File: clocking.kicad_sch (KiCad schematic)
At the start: 37 parts, among them J9 U.Fl, U2 LMK05318BRGZR, U21 TMP117xxDRV, U3 TG5032CGN

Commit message: Minor updates.
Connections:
- net VDDO_PLL2 renamed VDD_PLL2
- net VDDO_XO renamed VDD_XO
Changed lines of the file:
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@@
 		)
 	)
-	(text_box "The variant with filter cap appears to be vapour-ware."
+	(text_box "The variant with external filter cap appears to be vapour-ware."
 		(exclude_from_sim no)
-		(at 212.1153 31.8079 0)
-		(size 30.4547 5.0221)
+		(at 212.1153 43.2379 0)
+		(size 19.0247 10.1021)
 		(margins 0.9525 0.9525 0.9525 0.9525)
 		(stroke
@@
 		)
 	)
-	(label "VDDO_PLL2"
+	(label "VDD_PLL2"
 		(at 218.44 66.04 270)
 		(effects
@@
 		)
 	)
-	(label "VDDO_XO"
+	(label "VDD_XO"
 		(at 91.44 110.49 180)
 		(effects
@@
 		)
 	)
-	(label "VDDO_XO"
+	(label "VDD_XO"
 		(at 238.76 97.79 180)
 		(effects
@@
 		)
 	)
-	(label "VDDO_PLL2"
+	(label "VDD_PLL2"
 		(at 120.65 93.98 180)
 		(effects

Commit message: Minor tidy ups and fix a stupid bug.
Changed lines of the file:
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@@
 	)
 	(junction
+		(at 69.85 34.29)
+		(diameter 0)
+		(color 0 0 0 0)
+	)
+	(junction
 		(at 190.5 133.35)
 		(diameter 0)
@@
 	)
 	(junction
+		(at 69.85 74.93)
+		(diameter 0)
+		(color 0 0 0 0)
+	)
+	(junction
 		(at 96.52 48.26)
 		(diameter 0)
@@
 	)
 	(junction
-		(at 69.85 81.28)
-		(diameter 0)
-		(color 0 0 0 0)
-	)
-	(junction
 		(at 115.57 60.96)
 		(diameter 0)
@@
 	(wire
 		(pts
-			(xy 66.04 81.28) (xy 69.85 81.28)
+			(xy 66.04 74.93) (xy 69.85 74.93)
 		)
 		(stroke
@@
 	(wire
 		(pts
-			(xy 66.04 48.26) (xy 69.85 48.26)
+			(xy 66.04 34.29) (xy 69.85 34.29)
 		)
 		(stroke
@@
 	(wire
 		(pts
-			(xy 69.85 74.93) (xy 69.85 81.28)
-		)
-		(stroke
-			(width 0)
-			(type default)
-		)
-	)
-	(wire
-		(pts
 			(xy 227.33 113.03) (xy 238.76 113.03)
 		)
@@
 	(wire
 		(pts
-			(xy 69.85 81.28) (xy 69.85 88.9)
+			(xy 69.85 74.93) (xy 69.85 88.9)
 		)
 		(stroke
@@
 	(symbol
 		(lib_id "power:+1V8")
-		(at 66.04 48.26 0)
+		(at 66.04 34.29 0)
 		(unit 1)
 		(exclude_from_sim no)
@@
 		(dnp no)
 		(property "Reference" "#PWR062"
-			(at 66.04 52.07 0)
+			(at 66.04 38.1 0)
 			(effects
 				(font
@@
 		)
 		(property "Value" "+1V8"
-			(at 66.04 44.704 0)
+			(at 66.04 30.734 0)
 			(effects
 				(font
@@
 		)
 		(property "Footprint" ""
-			(at 66.04 48.26 0)
+			(at 66.04 34.29 0)
 			(effects
 				(font
@@
 		)
 		(property "Datasheet" ""
-			(at 66.04 48.26 0)
+			(at 66.04 34.29 0)
 			(effects
 				(font
@@
 		)
 		(property "Description" "Power symbol creates a global label with name \"+1V8\""
-			(at 66.04 48.26 0)
+			(at 66.04 34.29 0)
 			(effects
 				(font
@@
 	(symbol
 		(lib_id "power:+3V3")
-		(at 66.04 81.28 0)
+		(at 66.04 74.93 0)
 		(unit 1)
 		(exclude_from_sim no)
@@
 		(dnp no)
 		(property "Reference" "#PWR011"
-			(at 66.04 85.09 0)
+			(at 66.04 78.74 0)
 			(effects
 				(font
@@
 		)
 		(property "Value" "+3V3"
-			(at 66.04 77.724 0)
+			(at 66.04 71.374 0)
 			(effects
 				(font
@@
 		)
 		(property "Footprint" ""
-			(at 66.04 81.28 0)
+			(at 66.04 74.93 0)
 			(effects
 				(font
@@
 		)
 		(property "Datasheet" ""
-			(at 66.04 81.28 0)
+			(at 66.04 74.93 0)
 			(effects
 				(font
@@
 		)
 		(property "Description" "Power symbol creates a global label with name \"+3V3\""
-			(at 66.04 81.28 0)
+			(at 66.04 74.93 0)
 			(effects
 				(font

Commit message: Add LCSC part numbers for a few items.
Don't 'exclude from BOM' things we want to assemble.
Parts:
- C78: LCSC (none) -> C3855387; now in the parts list
- C92: LCSC (none) -> C20044553; now in the parts list
- U2, U3: now in the parts list
- U21: now not fitted
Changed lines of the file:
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@@
 		(in_bom no)
 		(on_board yes)
-		(dnp no)
+		(dnp yes)
 		(property "Reference" "U21"
 			(at 107.95 135.763 0)
@@
 		)
 		(instances
-			(project ""
+			(project "gpsfreak"
 				(path "/3160ff17-81c2-4674-af97-e8d9acaf6b65/131a3728-0d51-4d75-9961-26d31d87be39"
 					(reference "U21")
@@
 		)
 		(instances
-			(project ""
+			(project "gpsfreak"
 				(path "/3160ff17-81c2-4674-af97-e8d9acaf6b65/131a3728-0d51-4d75-9961-26d31d87be39"
 					(reference "#PWR062")
@@
 		(unit 1)
 		(exclude_from_sim no)
-		(in_bom no)
+		(in_bom yes)
 		(on_board yes)
 		(dnp no)
@@
 			)
 		)
+		(property "LCSC" "C3855387"
+			(at 243.84 133.35 0)
+			(effects
+				(font
+					(size 1.27 1.27)
+				)
+				(hide yes)
+			)
+		)
 		(pin "1"
 		)
@@
 		)
 		(instances
-			(project ""
+			(project "gpsfreak"
 				(path "/3160ff17-81c2-4674-af97-e8d9acaf6b65/131a3728-0d51-4d75-9961-26d31d87be39"
 					(reference "L26")
@@
 		(unit 1)
 		(exclude_from_sim no)
-		(in_bom no)
+		(in_bom yes)
 		(on_board yes)
 		(dnp no)
@@
 		)
 		(instances
-			(project ""
+			(project "gpsfreak"
 				(path "/3160ff17-81c2-4674-af97-e8d9acaf6b65/131a3728-0d51-4d75-9961-26d31d87be39"
 					(reference "R24")
@@
 		(unit 1)
 		(exclude_from_sim no)
-		(in_bom no)
+		(in_bom yes)
 		(on_board yes)
 		(dnp no)
@@
 		(unit 2)
 		(exclude_from_sim no)
-		(in_bom no)
+		(in_bom yes)
 		(on_board yes)
 		(dnp no)
@@
 		)
 		(instances
-			(project ""
+			(project "gpsfreak"
 				(path "/3160ff17-81c2-4674-af97-e8d9acaf6b65/131a3728-0d51-4d75-9961-26d31d87be39"
 					(reference "U3")
@@
 		(unit 1)
 		(exclude_from_sim no)
-		(in_bom no)
+		(in_bom yes)
 		(on_board yes)
 		(dnp no)
@@
 			(effects
 				(font
+					(size 1.27 1.27)
+				)
+				(hide yes)
+			)
+		)
+		(property "LCSC" "C20044553"
+			(at 245.11 95.25 90)
+			(effects
+				(font

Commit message: Tweaks to python scripts.
Add part numbers for the LED and 470nF C0G capacitor.
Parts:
- C79: LCSC (none) -> C21082486
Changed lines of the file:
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@@
 		)
 	)
+	(text_box "Temperature sensor is optional."
+		(exclude_from_sim no)
+		(at 125.73 134.62 0)
+		(size 20.32 4.768)
+		(margins 0.9525 0.9525 0.9525 0.9525)
+		(stroke
+			(width 0)
+			(type solid)
+		)
+		(fill
+			(type none)
+		)
+		(effects
+			(font
+				(size 1.27 1.27)
+			)
+			(justify left)
+		)
+	)
 	(text_box "GPIO1 selects I²C address."
 		(exclude_from_sim no)
@@
 			)
 		)
-		(property "Description" "Unpolarized capacitor"
+		(property "Description" "GRM31C5C1E474"
+			(at 251.46 133.35 0)
+			(effects
+				(font
+					(size 1.27 1.27)
+				)
+				(hide yes)
+			)
+		)
+		(property "LCSC" "C21082486"
 			(at 251.46 133.35 0)
 			(effects

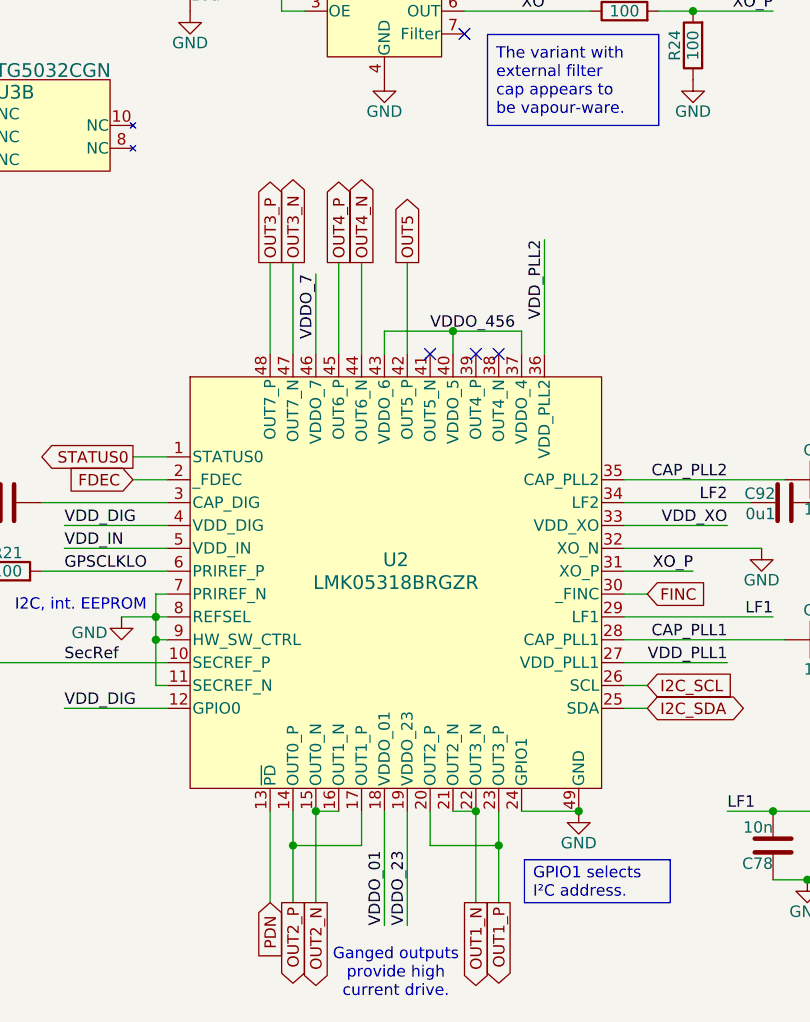
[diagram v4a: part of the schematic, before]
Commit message: Split each output onto it's own sheet.
Makes it easier to mix'n'match output types for board spins.
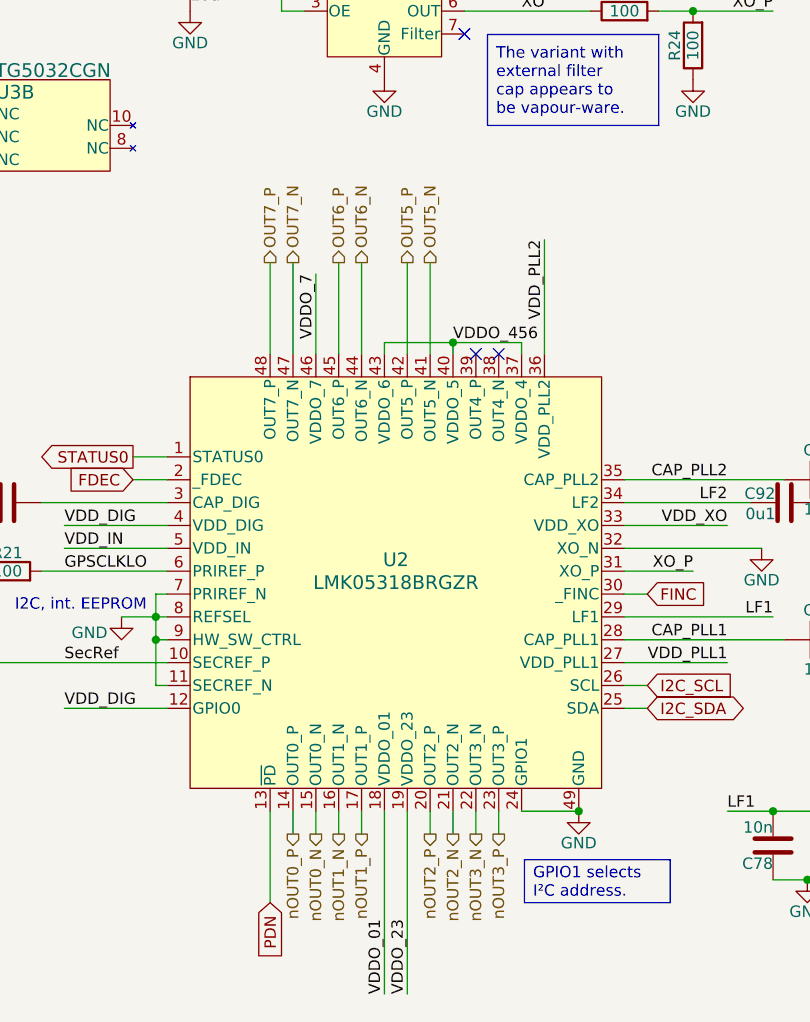
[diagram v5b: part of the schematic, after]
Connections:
- net OUT5_N: now reaches U2.41 (OUT5_N)
- net OUT1_N renamed nOUT2_N
- net nOUT2_N: no longer U2.22 (OUT3_N)
- net OUT1_P renamed nOUT2_P
- net nOUT2_P: no longer U2.23 (OUT3_P)
- net OUT2_N renamed nOUT0_N
- net nOUT0_N: no longer U2.16 (OUT1_N)
- net OUT2_P renamed nOUT0_P
- net nOUT0_P: no longer U2.17 (OUT1_P)
- net OUT3_N renamed OUT7_N
- net OUT3_P renamed OUT7_P
- net OUT4_N renamed OUT6_N
- net OUT4_P renamed OUT6_P
- net OUT5 renamed OUT5_P
- new net nOUT1_N: U2.16 (OUT1_N)
- new net nOUT1_P: U2.17 (OUT1_P)
- new net nOUT3_N: U2.22 (OUT3_N)
- new net nOUT3_P: U2.23 (OUT3_P)
- no-connect marks 4 -> 3
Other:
- note removed: "Ganged outputs provide high current drive."

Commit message: Touch up net names.
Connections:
- net OUT4_N: now reaches U2.38 (OUT4_N)
- net OUT4_P: now reaches U2.39 (OUT4_P)
- net nOUT0_N renamed OUT0_N
- net nOUT0_P renamed OUT0_P
- net nOUT1_N renamed OUT1_N
- net nOUT1_P renamed OUT1_P
- net nOUT2_N renamed OUT2_N
- net nOUT2_P renamed OUT2_P
- net nOUT3_N renamed OUT3_N
- net nOUT3_P renamed OUT3_P
- no-connect marks 3 -> 1
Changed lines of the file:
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@@
-	)
-	(no_connect
-		(at 213.36 78.74)
 	)
 	(no_connect
 		(at 209.55 43.18)
 	)
-	(no_connect
-		(at 210.82 78.74)
-	)
 	(wire
 		(pts
@@
 	(wire
 		(pts
-			(xy 205.74 68.58) (xy 205.74 78.74)
+			(xy 205.74 76.2) (xy 205.74 78.74)
 		)
 		(stroke
@@
 	(wire
 		(pts
-			(xy 195.58 78.74) (xy 195.58 68.58)
+			(xy 195.58 78.74) (xy 195.58 76.2)
 		)
 		(stroke
@@
 	(wire
 		(pts
+			(xy 213.36 76.2) (xy 213.36 78.74)
+		)
+		(stroke
+			(width 0)
+			(type default)
+		)
+	)
+	(wire
+		(pts
 			(xy 210.82 129.54) (xy 210.82 132.08)
 		)
@@
 	(wire
 		(pts
+			(xy 208.28 57.15) (xy 208.28 77.47)
+		)
+		(stroke
+			(width 0)
+			(type default)
+		)
+	)
+	(wire
+		(pts
 			(xy 254 95.25) (xy 254 110.49)
 		)
@@
 	(wire
 		(pts
-			(xy 190.5 78.74) (xy 190.5 68.58)
+			(xy 190.5 78.74) (xy 190.5 76.2)
 		)
 		(stroke
@@
 	(wire
 		(pts
-			(xy 193.04 78.74) (xy 193.04 69.85)
+			(xy 193.04 78.74) (xy 193.04 59.69)
 		)
 		(stroke
@@
 	(wire
 		(pts
-			(xy 203.2 68.58) (xy 203.2 78.74)
+			(xy 203.2 76.2) (xy 203.2 78.74)
 		)
 		(stroke
@@
 	(wire
 		(pts
-			(xy 198.12 78.74) (xy 198.12 68.58)
+			(xy 198.12 78.74) (xy 198.12 76.2)
 		)
 		(stroke
@@
 	(wire
 		(pts
-			(xy 187.96 78.74) (xy 187.96 68.58)
+			(xy 187.96 78.74) (xy 187.96 76.2)
 		)
 		(stroke
@@
 		(pts
 			(xy 107.95 146.05) (xy 119.38 146.05)
+		)
+		(stroke
+			(width 0)
+			(type default)
+		)
+	)
+	(wire
+		(pts
+			(xy 210.82 76.2) (xy 210.82 78.74)
 		)
 		(stroke
@@
 	)
 	(label "VDDO_456"
-		(at 208.28 77.47 0)
-		(effects
-			(font
-				(size 1.27 1.27)
-			)
-			(justify left bottom)
+		(at 208.28 57.15 270)
+		(effects
+			(font
+				(size 1.27 1.27)
+			)
+			(justify right bottom)
 		)
 	)
@@
 	)
 	(label "VDDO_7"
-		(at 193.04 69.85 270)
+		(at 193.04 59.69 270)
 		(effects
 			(font
@@
 	(hierarchical_label "OUT7_P"
 		(shape output)
-		(at 187.96 68.58 90)
+		(at 187.96 76.2 90)
 		(effects
 			(font
@@
 		)
 	)
-	(hierarchical_label "nOUT0_P"
+	(hierarchical_label "OUT0_P"
 		(shape output)
 		(at 190.5 132.08 270)
@@
 		)
 	)
-	(hierarchical_label "nOUT3_N"
+	(hierarchical_label "OUT3_N"
 		(shape output)
 		(at 210.82 132.08 270)
@@
 	(hierarchical_label "OUT6_N"
 		(shape output)
-		(at 198.12 68.58 90)
+		(at 198.12 76.2 90)
 		(effects
 			(font
@@
 		)
 	)
-	(hierarchical_label "nOUT2_N"
+	(hierarchical_label "OUT2_N"
 		(shape output)
 		(at 208.28 132.08 270)
@@
 		)
 	)
-	(hierarchical_label "nOUT2_P"
+	(hierarchical_label "OUT2_P"
 		(shape output)
 		(at 205.74 132.08 270)
@@
 	(hierarchical_label "OUT7_N"
 		(shape output)
-		(at 190.5 68.58 90)
+		(at 190.5 76.2 90)
 		(effects
 			(font
@@
 		)
 	)
-	(hierarchical_label "nOUT3_P"
+	(hierarchical_label "OUT4_N"
+		(shape output)
+		(at 213.36 76.2 90)
+		(effects
+			(font
+				(size 1.27 1.27)
+			)
+			(justify left)
+		)
+	)
+	(hierarchical_label "OUT3_P"
 		(shape output)
 		(at 213.36 132.08 270)
@@
 		)
 	)
-	(hierarchical_label "nOUT1_P"
+	(hierarchical_label "OUT1_P"
 		(shape output)
 		(at 198.12 132.08 270)
@@
 		)
 	)
-	(hierarchical_label "nOUT0_N"
+	(hierarchical_label "OUT4_P"
+		(shape output)
+		(at 210.82 76.2 90)
+		(effects
+			(font
+				(size 1.27 1.27)
+			)
+			(justify left)
+		)
+	)
+	(hierarchical_label "OUT0_N"
 		(shape output)
 		(at 193.04 132.08 270)
@@
 	(hierarchical_label "OUT5_N"
 		(shape output)
-		(at 205.74 68.58 90)
+		(at 205.74 76.2 90)
 		(effects
 			(font
@@
 		)
 	)
-	(hierarchical_label "nOUT1_N"
+	(hierarchical_label "OUT1_N"
 		(shape output)
 		(at 195.58 132.08 270)
@@
 	(hierarchical_label "OUT5_P"
 		(shape output)
-		(at 203.2 68.58 90)
+		(at 203.2 76.2 90)
 		(effects
 			(font
@@
 	(hierarchical_label "OUT6_P"
 		(shape output)
-		(at 195.58 68.58 90)
-		(effects
-			(font
+		(at 195.58 76.2 90)
+		(effects
+			(font

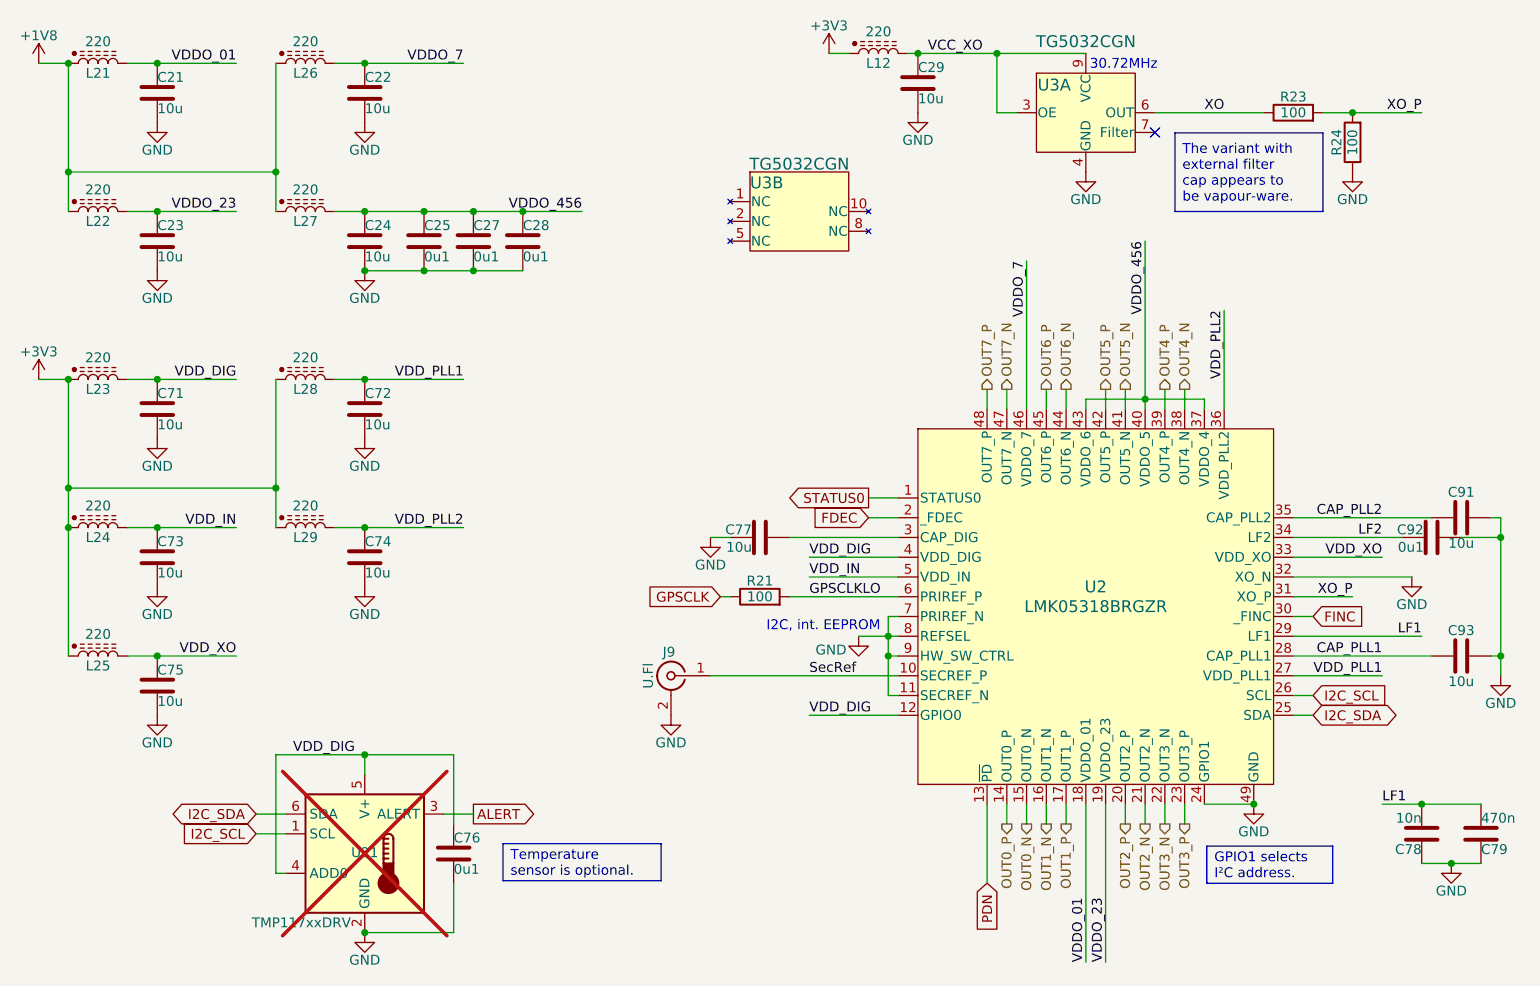
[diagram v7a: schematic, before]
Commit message: FPGA in, layout mostly updated.
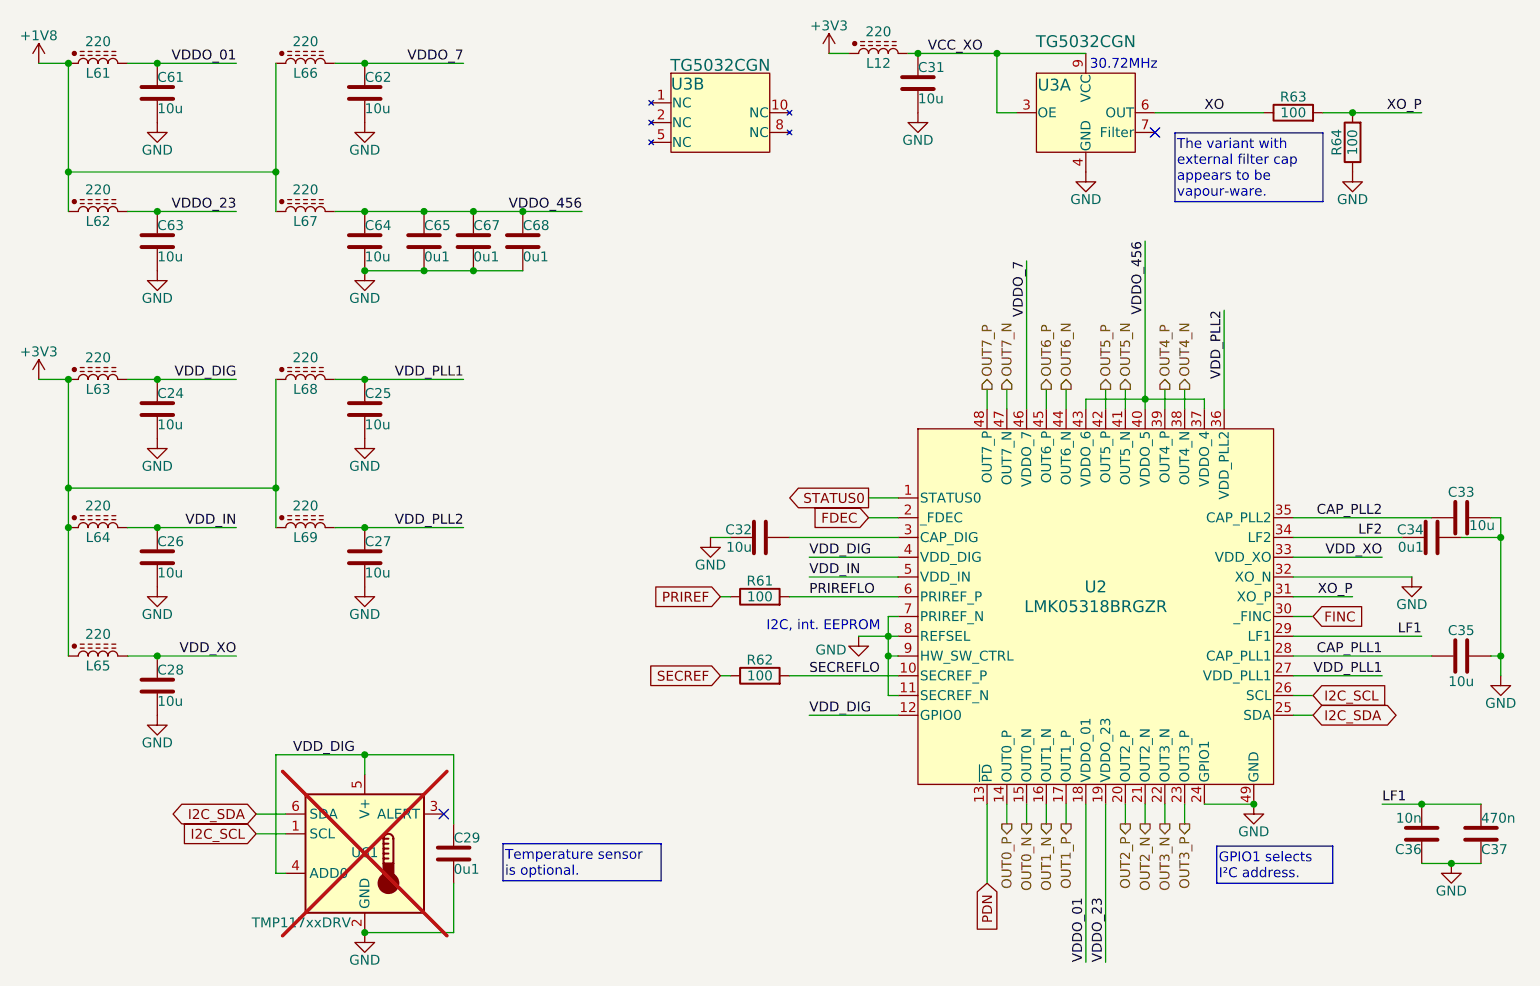
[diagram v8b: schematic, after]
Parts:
- removed J9: U.Fl, Parts:U.FL_Hirose_U.FL-R-SMT-1_Vertical, symbol Connector:Conn_Coaxial
- added R62: 100, Resistor_SMD:R_0402_1005Metric, symbol Device:R
- renumbered C71 to C24, C72 to C25, C73 to C26, C74 to C27, C75 to C28, C76 to C29, C29 to C31, C77 to C32, C91 to C33, C92 to C34, C93 to C35, C78 to C36, C79 to C37, C21 to C61, C22 to C62, C23 to C63, C24 to C64, C25 to C65, C27 to C67, C28 to C68, L21 to L61, L22 to L62, L23 to L63, L24 to L64, L25 to L65, L26 to L66, L27 to L67, L28 to L68, L29 to L69, R21 to R61, R23 to R63, R24 to R64, U21 to U61
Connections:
- net ALERT: no longer names the net of U61.3 (ALERT)
- net GPSCLK renamed PRIREF
- net GPSCLKLO renamed PRIREFLO
- net SecRef renamed SECREFLO
- net SECREFLO: now also R62.2
- new net SECREF: R62.1
- no-connect marks 1 -> 2
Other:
- moved on the sheet: U3B
